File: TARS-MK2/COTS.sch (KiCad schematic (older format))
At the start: 0 parts

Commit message: completed COTS schematics
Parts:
- added U1: StratoLogger, symbol COTS_Altimeters:StratoLogger
- added U2: TeleMetrum, symbol COTS_Altimeters:TeleMetrum
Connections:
- new net SL_DROGUE_0: U1.6 (DROGUE1)
- new net SL_DROGUE_1: U1.5 (DROGUE0)
- new net SL_POWER_NEGATIVE: U1.4 (NEGATIVE)
- new net SL_POWER_POSITIVE: U1.3 (POSITIVE)
- new net SL_SWITCH_0: U1.1 (SWITCH0)
- new net SL_SWITCH_1: U1.2 (SWITCH1)
- new net TM_DROGUE_0: U2.7 (DROGUE0)
- new net TM_DROGUE_1: U2.8 (DROGUE1)
- new net TM_POWER_NEGATIVE: U2.2 (NEGATIVE)
- new net TM_POWER_POSITIVE: U2.1 (POSITIVE)
- new net TM_SWITCH_0: U2.3 (SWITCH0)
- new net TM_SWITCH_1: U2.4 (SWITCH1)
- no-connect marks 0 -> 4
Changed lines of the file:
@@
 $Descr A4 11693 8268
 encoding utf-8
-Sheet 7 8
+Sheet 8 8
 Title ""
 Date ""
@@
 P 7700 6800
 AR Path="/600297E0" Ref="#G?"  Part="1"
-AR Path="/60021DCE/600297E0" Ref="#G?"  Part="1"
-F 0 "#G?" H 7700 6677 60  0001 C CNN
+AR Path="/60021DCE/600297E0" Ref="#G7"  Part="1"
+F 0 "#G7" H 7700 6677 60  0001 C CNN
 F 1 "LOGO" H 7700 6923 60  0001 C CNN
 F 2 "" H 7700 6800 50  0001 C CNN
@@
 	1    0    0    -1
 $EndComp
+Text HLabel 4550 2350 0    50   BiDi ~ 0
+SL_SWITCH_0
+Text HLabel 4550 2450 0    50   BiDi ~ 0
+SL_SWITCH_1
+Text HLabel 4800 4800 3    50   BiDi ~ 0
+TM_SWITCH_0
+Text HLabel 4900 4800 3    50   BiDi ~ 0
+TM_SWITCH_1
+Text HLabel 5650 2450 2    50   BiDi ~ 0
+SL_DROGUE_0
+Text HLabel 5650 2350 2    50   BiDi ~ 0
+SL_DROGUE_1
+Text HLabel 5300 4800 3    50   BiDi ~ 0
+TM_DROGUE_0
+$Comp
+L COTS_Altimeters:StratoLogger U1
+U 1 1 6004A99D
+P 5100 1900
+F 0 "U1" H 5100 2265 50  0000 C CNN
+F 1 "StratoLogger" H 5100 2174 50  0000 C CNN
+F 2 "" H 5100 2300 50  0001 C CNN
+F 3 "" H 5100 2300 50  0001 C CNN
+	1    5100 1900
+	1    0    0    -1
+$EndComp
+$Comp
+L COTS_Altimeters:TeleMetrum U2
+U 1 1 60052DB4
+P 5100 3750
+F 0 "U2" H 5578 3363 50  0000 L CNN
+F 1 "TeleMetrum" H 5578 3272 50  0000 L CNN
+F 2 "" H 5100 4150 50  0001 C CNN
+F 3 "" H 5100 4150 50  0001 C CNN
+	1    5100 3750
+	1    0    0    -1
+$EndComp
+Text HLabel 4550 2600 0    50   BiDi ~ 0
+SL_POWER_POSITIVE
+Text HLabel 4550 2700 0    50   BiDi ~ 0
+SL_POWER_NEGATIVE
+NoConn ~ 5650 2600
+NoConn ~ 5650 2700
+NoConn ~ 5050 4800
+NoConn ~ 5150 4800
+Text HLabel 4550 4100 0    50   BiDi ~ 0
+TM_POWER_NEGATIVE
+Text HLabel 4550 4000 0    50   BiDi ~ 0
+TM_POWER_POSITIVE
+Text HLabel 5400 4800 3    50   BiDi ~ 0
+TM_DROGUE_1
 $EndSCHEMATC

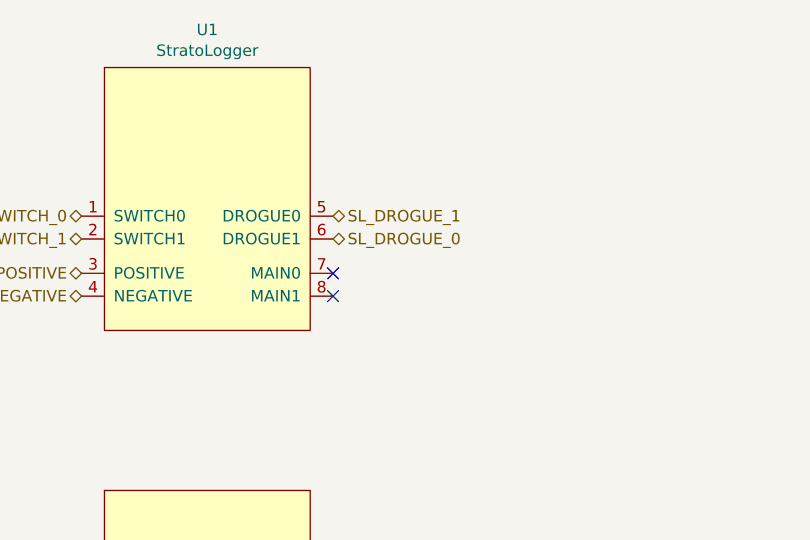
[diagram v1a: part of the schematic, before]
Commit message: fixed schematic for COTS
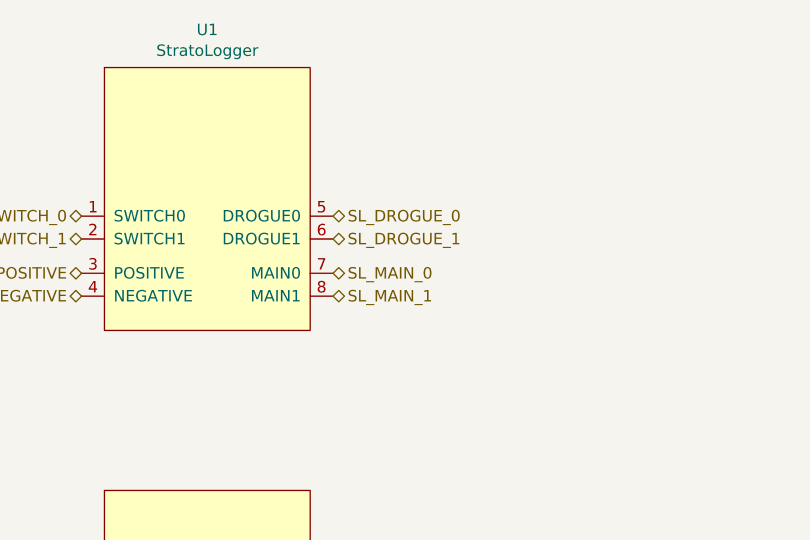
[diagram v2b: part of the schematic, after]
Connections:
- net SL_DROGUE_0: now also U1.5 (DROGUE0); no longer U1.6 (DROGUE1)
- net SL_DROGUE_1: now also U1.6 (DROGUE1); no longer U1.5 (DROGUE0)
- net SL_MAIN_0: now reaches U1.7 (MAIN0)
- net SL_MAIN_1: now reaches U1.8 (MAIN1)
- no-connect marks 4 -> 2
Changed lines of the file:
@@
 Text HLabel 4900 4800 3    50   BiDi ~ 0
 TM_SWITCH_1
-Text HLabel 5650 2450 2    50   BiDi ~ 0
+Text HLabel 5650 2350 2    50   BiDi ~ 0
 SL_DROGUE_0
-Text HLabel 5650 2350 2    50   BiDi ~ 0
-SL_DROGUE_1
 Text HLabel 5300 4800 3    50   BiDi ~ 0
 TM_DROGUE_0
@@
 Text HLabel 4550 2700 0    50   BiDi ~ 0
 SL_POWER_NEGATIVE
-NoConn ~ 5650 2600
-NoConn ~ 5650 2700
 NoConn ~ 5050 4800
 NoConn ~ 5150 4800
@@
 Text HLabel 5400 4800 3    50   BiDi ~ 0
 TM_DROGUE_1
+Text HLabel 5650 2600 2    50   BiDi ~ 0
+SL_MAIN_0
+Text HLabel 5650 2700 2    50   BiDi ~ 0
+SL_MAIN_1
+Text HLabel 5650 2450 2    50   BiDi ~ 0
+SL_DROGUE_1
 $EndSCHEMATC

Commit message: COTS ironed out
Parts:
- removed U1: StratoLogger, symbol COTS_Altimeters:StratoLogger
- removed U2: TeleMetrum, symbol COTS_Altimeters:TeleMetrum
- added A1: StratoLogger, COTS_Altimeters:StratoLogger, symbol COTS_Altimeters:StratoLogger
- added A2: TeleMetrum, COTS_Altimeters:TeleMetrum, symbol COTS_Altimeters:TeleMetrum
- added J1, J2, J3, J4, J5, J6: 505575-0271, 505575-0271:505575-0271, symbol 505575-0271:505575-0271
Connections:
- new net: A1.1 (SWITCH0), J1.1
- new net: A1.2 (SWITCH1), J1.2
- new net: A1.5 (DROGUE0), J6.1
- new net: A1.6 (DROGUE1), J6.2
- new net: A1.7 (MAIN0), J5.1
- new net: A1.8 (MAIN1), J5.2
- new net: A2.3 (SWITCH0), J2.1
- new net: A2.4 (SWITCH1), J2.2
- new net: A2.5 (MAIN0), J3.1
- new net: A2.6 (MAIN1), J3.2
- new net: A2.7 (DROGUE0), J4.1
- new net: A2.8 (DROGUE1), J4.2
- new net GND: A1.4 (NEGATIVE), A2.2 (NEGATIVE), J1.3, J1.4, J2.3, J2.4, J3.3, J3.4, J4.3, J4.4, J5.3, J5.4, J6.3, J6.4
- new net SL_POWER: A1.3 (POSITIVE)
- new net TM_POWER: A2.1 (POSITIVE)
- no-connect marks 2 -> 0

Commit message: meeting notes
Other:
- note added: "check with molex to see if there is a Thru-hole mount\n"
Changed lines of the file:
@@
 	1    0    0    -1
 $EndComp
+Text Notes 6400 3500 0    50   ~ 0
+check with molex to see if there is a Thru-hole mount\n
 $EndSCHEMATC

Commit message: begin PCB schematics for COTS
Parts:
- added J7: SL_BATT_0, Connector_JST:JST_PH_B2B-PH-K_1x02_P2.00mm_Vertical, symbol Connector_Generic:Conn_01x02
- added J8: SL_BATT_1, Connector_JST:JST_PH_B2B-PH-K_1x02_P2.00mm_Vertical, symbol Connector_Generic:Conn_01x02
- added J9: TM_BATT_0, Connector_JST:JST_PH_B2B-PH-K_1x02_P2.00mm_Vertical, symbol Connector_Generic:Conn_01x02
- J1: value 505575-0271 -> SL_SWITCH
- J2: value 505575-0271 -> TM_SWITCH
- J3: value 505575-0271 -> TM_MAIN
- J4: value 505575-0271 -> TM_DROGUE
- J5: value 505575-0271 -> SL_MAIN
- J6: value 505575-0271 -> SL_DROGUE
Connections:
- net GND: now also J8.2 (Pin_2), J9.2 (Pin_2); no longer J1.3, J1.4, J2.3, J2.4, J3.3, J3.4, J4.3, J4.4, J5.3, J5.4, J6.3, J6.4
- net SL_POWER renamed SL_POWER_POSITIVE
- net SL_POWER_POSITIVE: now also J7.1 (Pin_1)
- net TM_POWER renamed TM_POWER_POSITIVE
- net TM_POWER_POSITIVE: now also J9.1 (Pin_1)
- new net: J7.2 (Pin_2), J8.1 (Pin_1)
- no-connect marks 0 -> 12
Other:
- note added: "3 x 450 mAh Batteries"
- note removed: "check with molex to see if there is a Thru-hole mount\n"
- moved on the sheet: A1, A2, J1
